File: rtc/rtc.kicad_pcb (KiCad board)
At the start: 2 copper layers, 23.5 x 32.4 mm, 17 parts, among them J1 Conn_02x03_Odd_Even, J2 Conn_01x04, J3 Conn_01x04, J4 Conn_01x04, U1 PCF8563T/5_518, Y1 LFXTAL016178REEL

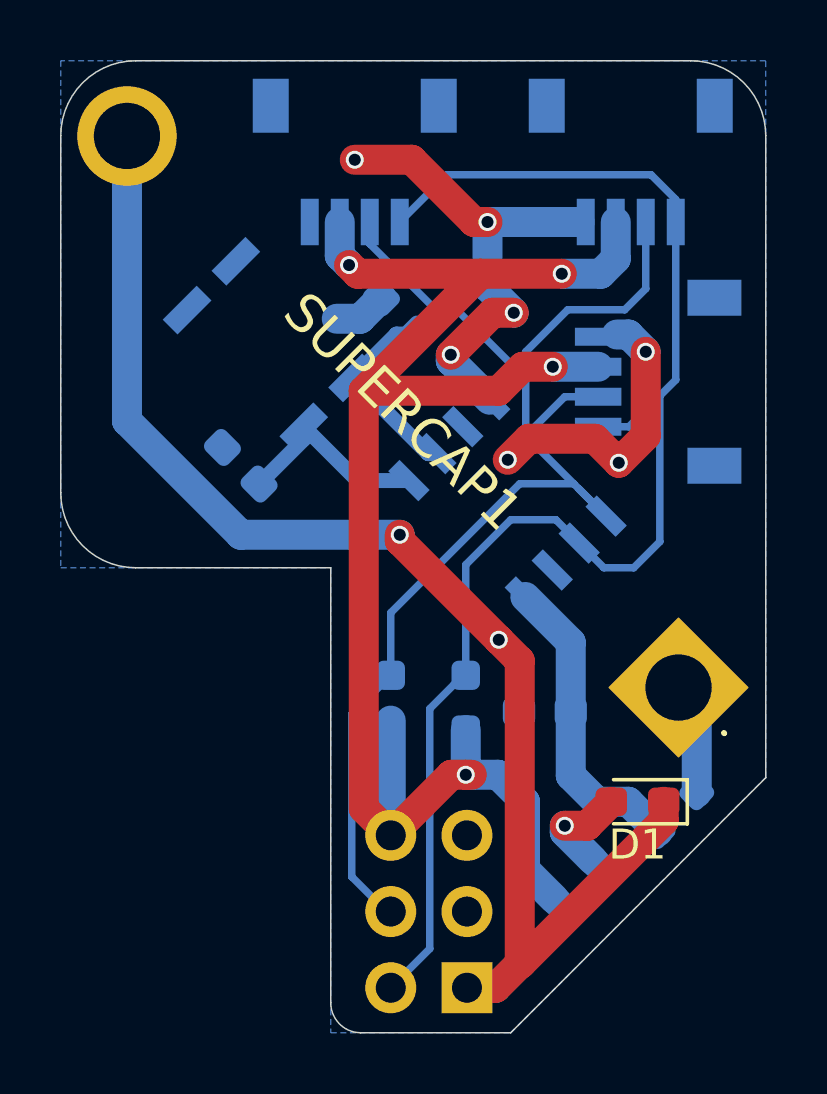
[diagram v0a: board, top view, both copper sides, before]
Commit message: new RTC
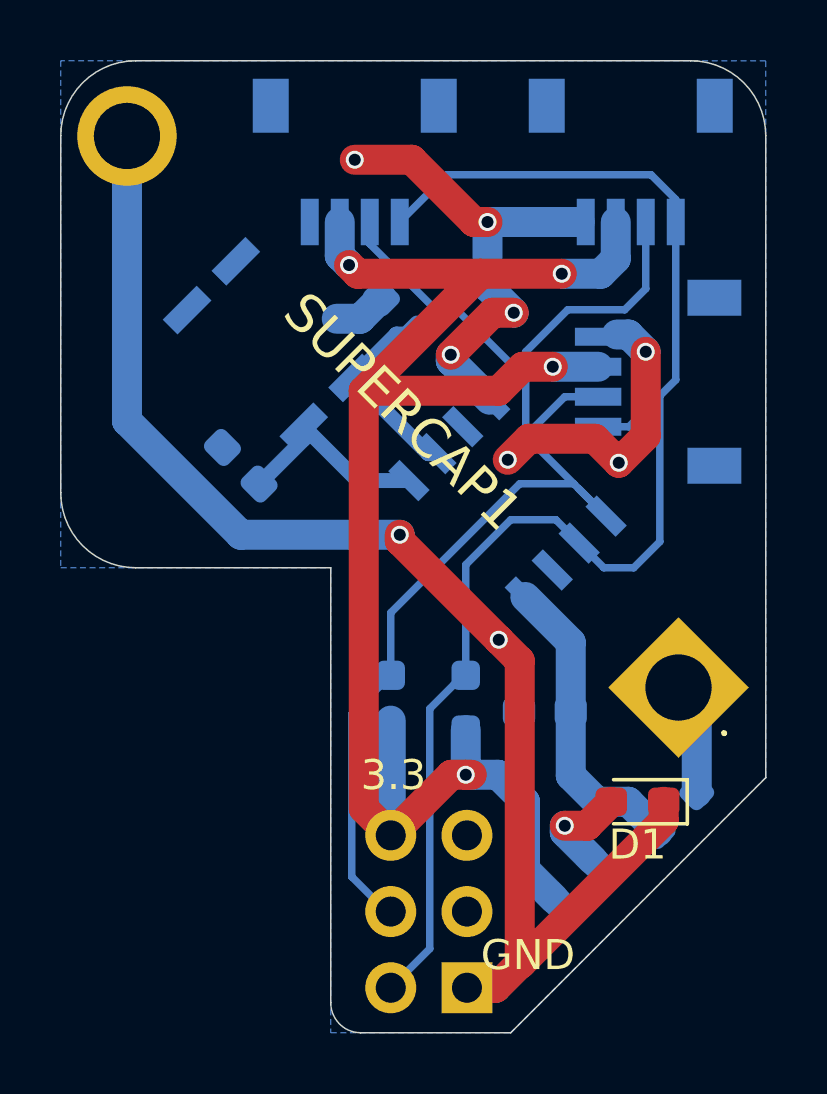
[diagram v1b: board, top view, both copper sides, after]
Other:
- board text added: "3.3"
- board text added: "GND"
